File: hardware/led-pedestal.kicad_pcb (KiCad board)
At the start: 2 copper layers, 24 x 24 mm, 29 parts, among them J1 USB_B_Micro, J2 ISP, Q1 AO3401A, SW1 SKRPACE010, U1 LTC4054ES5-4.2, U2 FS8205A, U3 FS312F-G, U4 XC6206PxxxMR, U5 PIC10F222-IOT

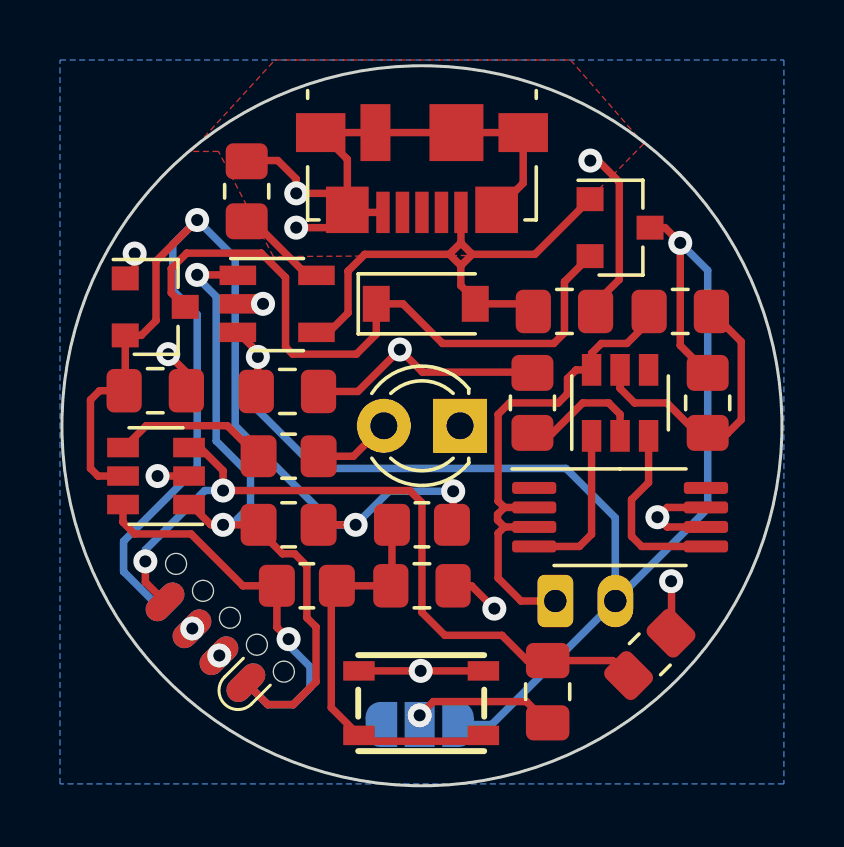
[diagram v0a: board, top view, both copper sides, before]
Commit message: Add revision 2 of the hardware
Changes include:
- moved button to the center for better fit of the case
- added silkscreen marks for + and minus of the LED
- connect jumper to battery measurement variant
- lower charging current (from 100 to 30 mA)
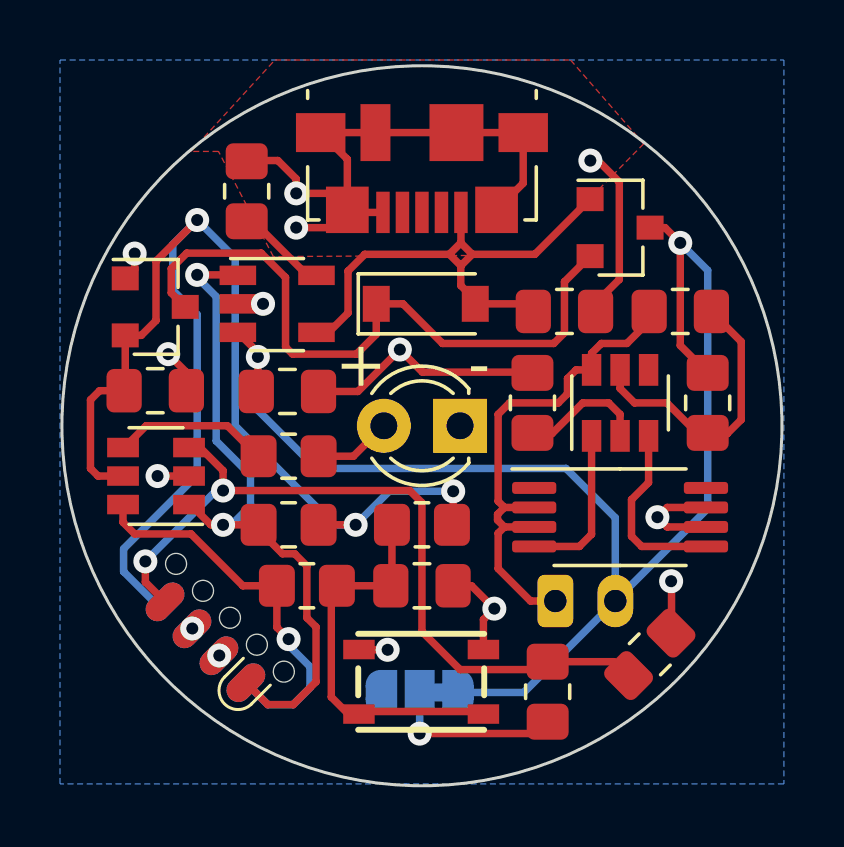
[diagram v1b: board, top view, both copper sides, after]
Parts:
- removed C3: TBD, Capacitor_SMD:C_0805_2012Metric_Pad1.18x1.45mm_HandSolder
- removed TH1: TBD, Resistor_SMD:R_0805_2012Metric_Pad1.20x1.40mm_HandSolder
- added R8: 33k, Resistor_SMD:R_0805_2012Metric_Pad1.20x1.40mm_HandSolder, F.Cu at (155.5, 102.4)
- added R9: 10k, Resistor_SMD:R_0805_2012Metric_Pad1.20x1.40mm_HandSolder, F.Cu at (152.1, 103.6)
- JP1: footprint Jumper:SolderJumper-3_P1.3mm_Open_RoundedPad1.0x1.5mm -> Jumper:SolderJumper-3_P1.3mm_Bridged12_RoundedPad1.0x1.5mm_NumberLabels
- R1: value 10k -> 33k
- R5: value 56 -> 68
- R6: value 470 -> 100
- U1: value LTC4054ES5-4.2 -> LTC4054|TP4054
- moved JP1 1.07 mm to (147.9, 103.6), turned to 180 degrees
- moved SW1 0.71 mm to (147.9, 103.3)
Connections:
- J1 pad 2: no_connect_19 -> unconnected-(J1-Pad2)
- J1 pad 3: no_connect_20 -> unconnected-(J1-Pad3)
- J1 pad 4: no_connect_21 -> unconnected-(J1-Pad4)
- JP1 pad 1: GND -> +BATT
- JP1 pad 3: +BATT -> GND
- U2 pad 1: no_connect_22 -> unconnected-(U2-Pad1)
- U2 pad 8: no_connect_23 -> unconnected-(U2-Pad8)
- U3 pad 4: (no net) -> unconnected-(U3-Pad4)
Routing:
- net GND: track 49.8 -> 48.1 mm
- net Net-(JP1-Pad2): track 5.11 -> 6.22 mm
- net Net-(C5-Pad1): track 13.6 -> 13.0 mm
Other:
- board text added: "+"
- board text added: "-"

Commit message: Re-export correct files for revision 2 of the PCB
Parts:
- SW1: value SKRPACE010 -> VAL**
